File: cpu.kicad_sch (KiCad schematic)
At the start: 22 parts, among them IC1 68HC000

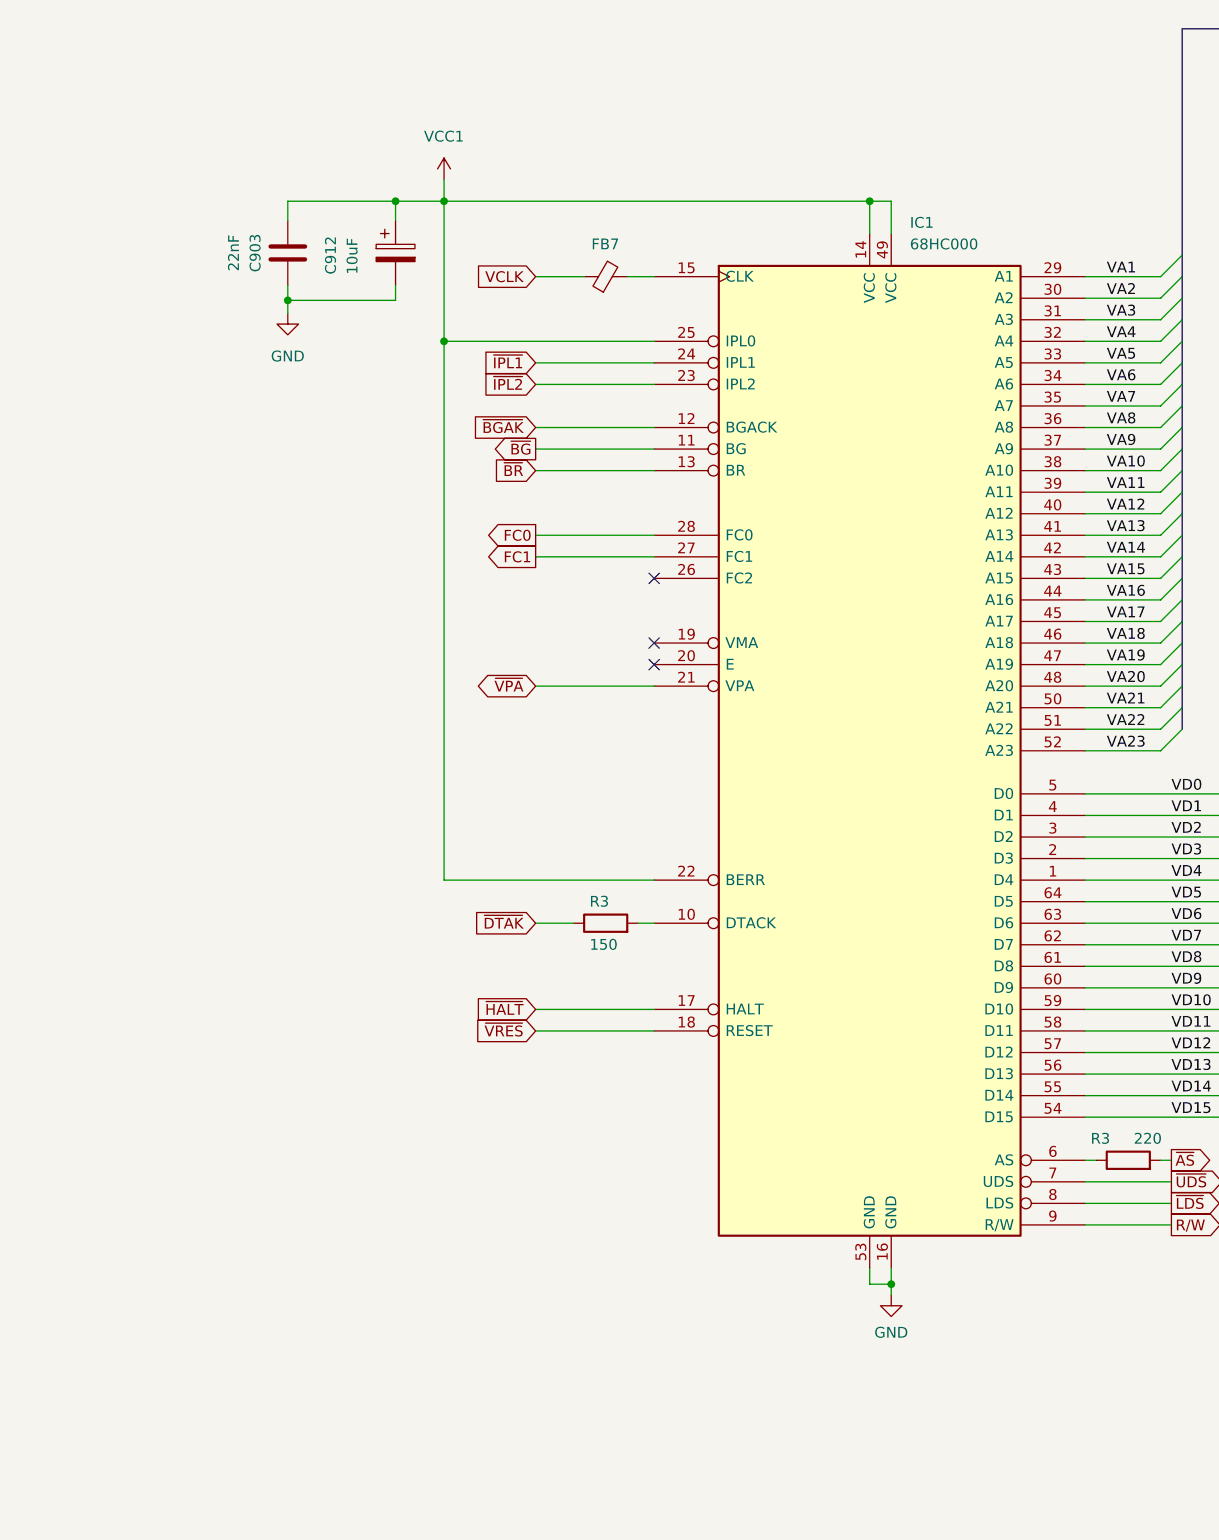
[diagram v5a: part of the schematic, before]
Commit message: Correct M68K pinout.
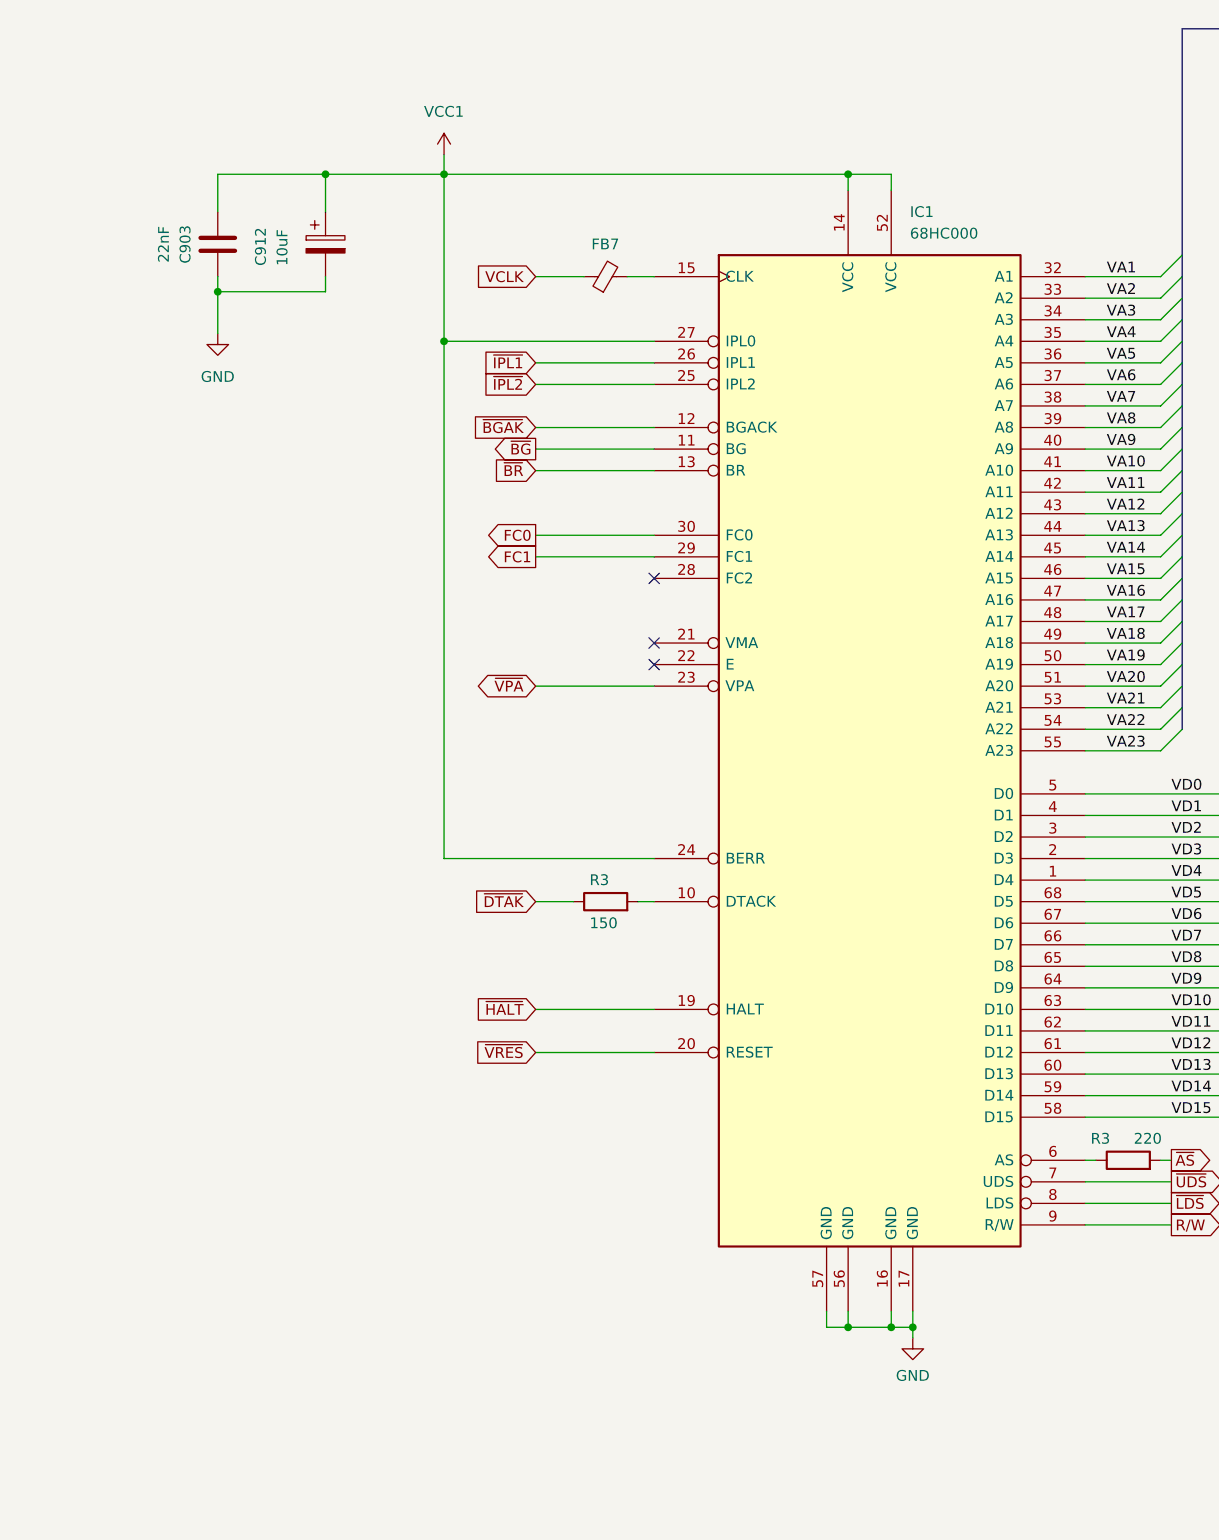
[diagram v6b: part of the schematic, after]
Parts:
- IC1: symbol CPU_NXP_68000:68000D -> CPU_NXP_68000:MC68000FN
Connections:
- net FC0: now also IC1.30 (FC0); no longer IC1.28 (FC0)
- net FC1: now also IC1.29 (FC1); no longer IC1.27 (FC1)
- net GND: now also IC1.17 (GND), IC1.56 (GND), IC1.57 (GND); no longer IC1.53 (GND)
- net VA1: now also IC1.32 (A1); no longer IC1.29 (A1)
- net VA10: now also IC1.41 (A10); no longer IC1.38 (A10)
- net VA11: now also IC1.42 (A11); no longer IC1.39 (A11)
- net VA12: now also IC1.43 (A12); no longer IC1.40 (A12)
- net VA13: now also IC1.44 (A13); no longer IC1.41 (A13)
- net VA14: now also IC1.45 (A14); no longer IC1.42 (A14)
- net VA15: now also IC1.46 (A15); no longer IC1.43 (A15)
- net VA16: now also IC1.47 (A16); no longer IC1.44 (A16)
- net VA17: now also IC1.48 (A17); no longer IC1.45 (A17)
- net VA18: now also IC1.49 (A18); no longer IC1.46 (A18)
- net VA19: now also IC1.50 (A19); no longer IC1.47 (A19)
- net VA2: now also IC1.33 (A2); no longer IC1.30 (A2)
- net VA20: now also IC1.51 (A20); no longer IC1.48 (A20)
- net VA21: now also IC1.53 (A21); no longer IC1.50 (A21)
- net VA22: now also IC1.54 (A22); no longer IC1.51 (A22)
- net VA23: now also IC1.55 (A23); no longer IC1.52 (A23)
- net VA3: now also IC1.34 (A3); no longer IC1.31 (A3)
- net VA4: now also IC1.35 (A4); no longer IC1.32 (A4)
- net VA5: now also IC1.36 (A5); no longer IC1.33 (A5)
- net VA6: now also IC1.37 (A6); no longer IC1.34 (A6)
- net VA7: now also IC1.38 (A7); no longer IC1.35 (A7)
- net VA8: now also IC1.39 (A8); no longer IC1.36 (A8)
- net VA9: now also IC1.40 (A9); no longer IC1.37 (A9)
- net VCC1: now also IC1.24 (BERR), IC1.27 (IPL0), IC1.52 (VCC); no longer IC1.22 (BERR), IC1.25 (IPL0), IC1.49 (VCC)
- net VD10: now also IC1.63 (D10); no longer IC1.59 (D10)
- net VD11: now also IC1.62 (D11); no longer IC1.58 (D11)
- net VD12: now also IC1.61 (D12); no longer IC1.57 (D12)
- net VD13: now also IC1.60 (D13); no longer IC1.56 (D13)
- net VD14: now also IC1.59 (D14); no longer IC1.55 (D14)
- net VD15: now also IC1.58 (D15); no longer IC1.54 (D15)
- net VD5: now also IC1.68 (D5); no longer IC1.64 (D5)
- net VD6: now also IC1.67 (D6); no longer IC1.63 (D6)
- net VD7: now also IC1.66 (D7); no longer IC1.62 (D7)
- net VD8: now also IC1.65 (D8); no longer IC1.61 (D8)
- net VD9: now also IC1.64 (D9); no longer IC1.60 (D9)
- net ~{HALT}: now also IC1.19 (HALT); no longer IC1.17 (HALT)
- net ~{IPL1}: now also IC1.26 (IPL1); no longer IC1.24 (IPL1)
- net ~{IPL2}: now also IC1.25 (IPL2); no longer IC1.23 (IPL2)
- net ~{VPA}: now also IC1.23 (VPA); no longer IC1.21 (VPA)
- net ~{VRES}: now also IC1.20 (RESET); no longer IC1.18 (RESET)
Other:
- moved on the sheet: C903, C912, R3

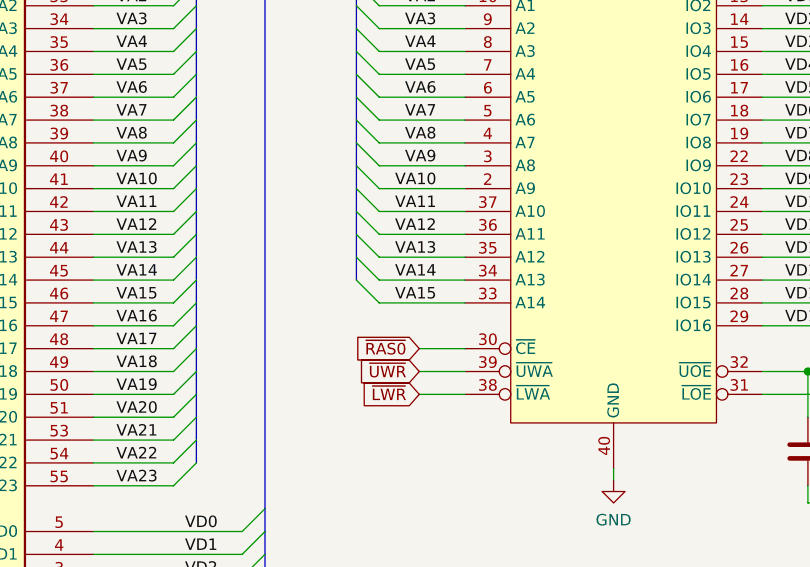
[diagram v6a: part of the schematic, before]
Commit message: SMS compatibility fixes.
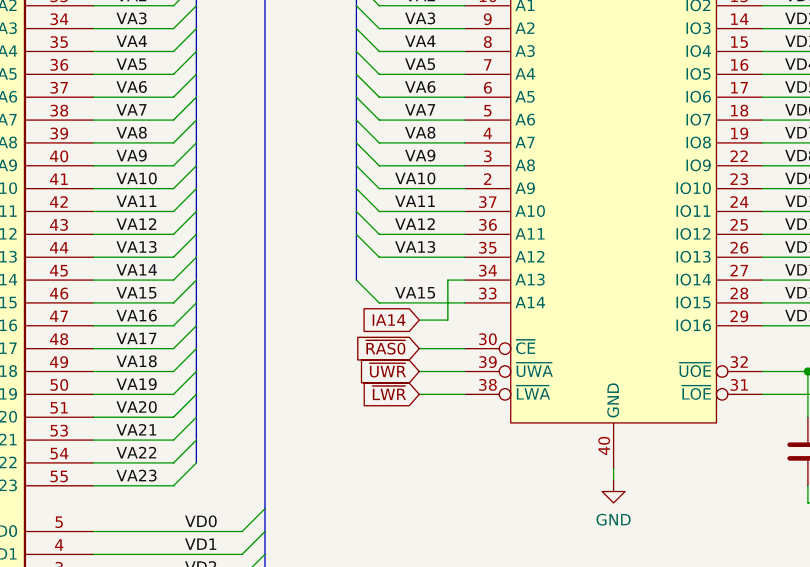
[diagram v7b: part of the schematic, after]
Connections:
- net VA14: no longer IC2.34 (A13)
- new net IA14: IC2.34 (A13)
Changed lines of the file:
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@@
-    (stroke (width 0) (type default))
-  )
-  (bus_entry (at 223.52 92.71) (size -2.54 -2.54)
     (stroke (width 0) (type default))
   )
@@
     (stroke (width 0) (type default))
   )
-  (bus (pts (xy 220.98 92.71) (xy 220.98 90.17))
+  (bus (pts (xy 220.98 87.63) (xy 220.98 92.71))
     (stroke (width 0) (type default))
   )
@@
     (stroke (width 0) (type default))
   )
-  (wire (pts (xy 223.52 92.71) (xy 233.045 92.71))
-    (stroke (width 0) (type default))
-  )
   (bus (pts (xy 272.415 186.055) (xy 272.415 183.515))
     (stroke (width 0) (type default))
@@
     (stroke (width 0) (type default))
   )
-  (bus (pts (xy 220.98 90.17) (xy 220.98 87.63))
-    (stroke (width 0) (type default))
-  )
   (wire (pts (xy 266.065 95.25) (xy 274.955 95.25))
     (stroke (width 0) (type default))
@@
     (stroke (width 0) (type default))
   )
+  (wire (pts (xy 231.14 92.71) (xy 231.14 97.155))
+    (stroke (width 0) (type default))
+  )
   (wire (pts (xy 165.735 241.3) (xy 165.735 243.84))
     (stroke (width 0) (type default))
   )
+  (wire (pts (xy 233.045 92.71) (xy 231.14 92.71))
+    (stroke (width 0) (type default))
+  )
   (bus (pts (xy 332.105 180.975) (xy 332.105 178.435))
     (stroke (width 0) (type default))
@@
   )
   (bus (pts (xy 277.495 36.195) (xy 210.82 36.195))
+    (stroke (width 0) (type default))
+  )
+  (wire (pts (xy 231.14 97.155) (xy 227.965 97.155))
     (stroke (width 0) (type default))
   )
@@
   (label "SD6" (at 321.31 188.595 0) (fields_autoplaced)
     (effects (font (size 1.27 1.27)) (justify left bottom))
-  )
-  (label "VA14" (at 229.87 92.71 180) (fields_autoplaced)
-    (effects (font (size 1.27 1.27)) (justify right bottom))
   )
   (label "VA3" (at 194.31 64.77 0) (fields_autoplaced)
@@
       (effects (font (size 1.27 1.27)) (justify right) hide)
     )
+  )
+  (global_label "IA14" (shape input) (at 227.965 97.155 180) (fields_autoplaced)
+    (effects (font (size 1.27 1.27)) (justify right))
+    (property "Intersheetrefs" "${INTERSHEET_REFS}" (at 220.8674 97.155 0)
+      (effects (font (size 1.27 1.27)) (justify right) hide)
+    )
